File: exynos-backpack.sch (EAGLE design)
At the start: 53 parts, among them IC1 MIC5335-SPYMT, IC2 TXS0108ERGY, IC3 LTC4352DD, IC4 LTC4352DD, IC5 LTC4352DD, Q1 SI7234DP, Q2 SI7234DP, Q3 SI7234DP

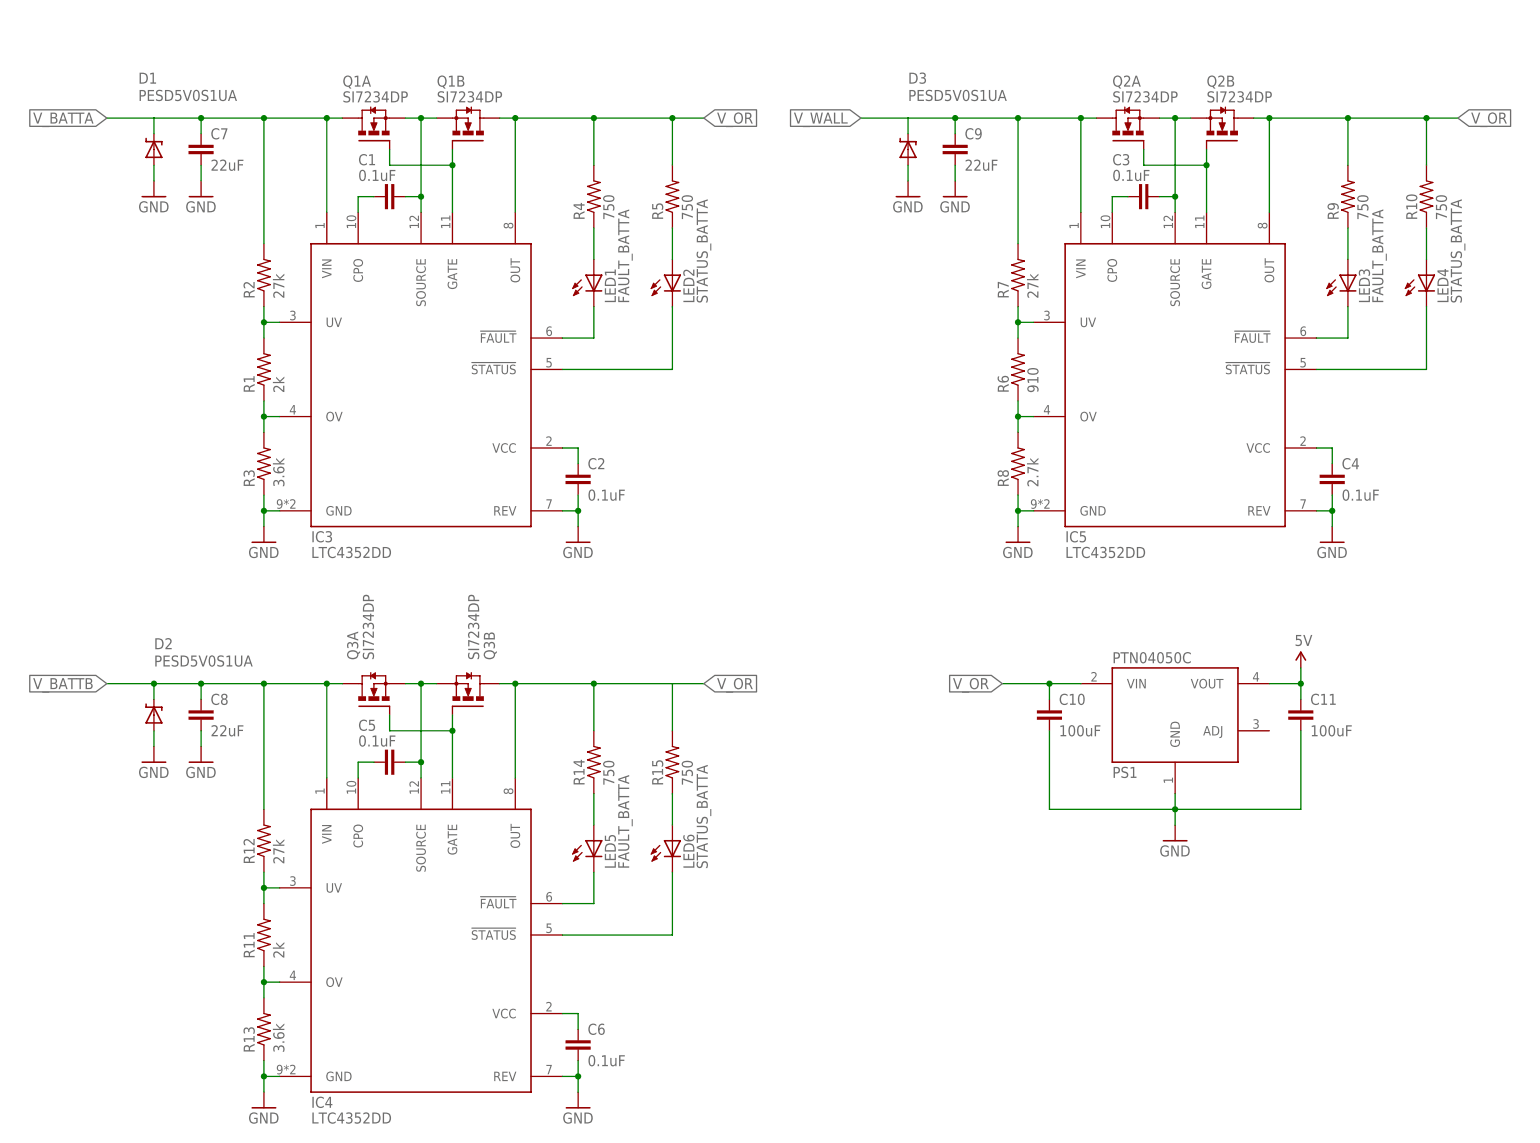
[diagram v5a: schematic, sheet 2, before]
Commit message: Adjust Rlim on LiPo ideal-OR LEDs down to 330
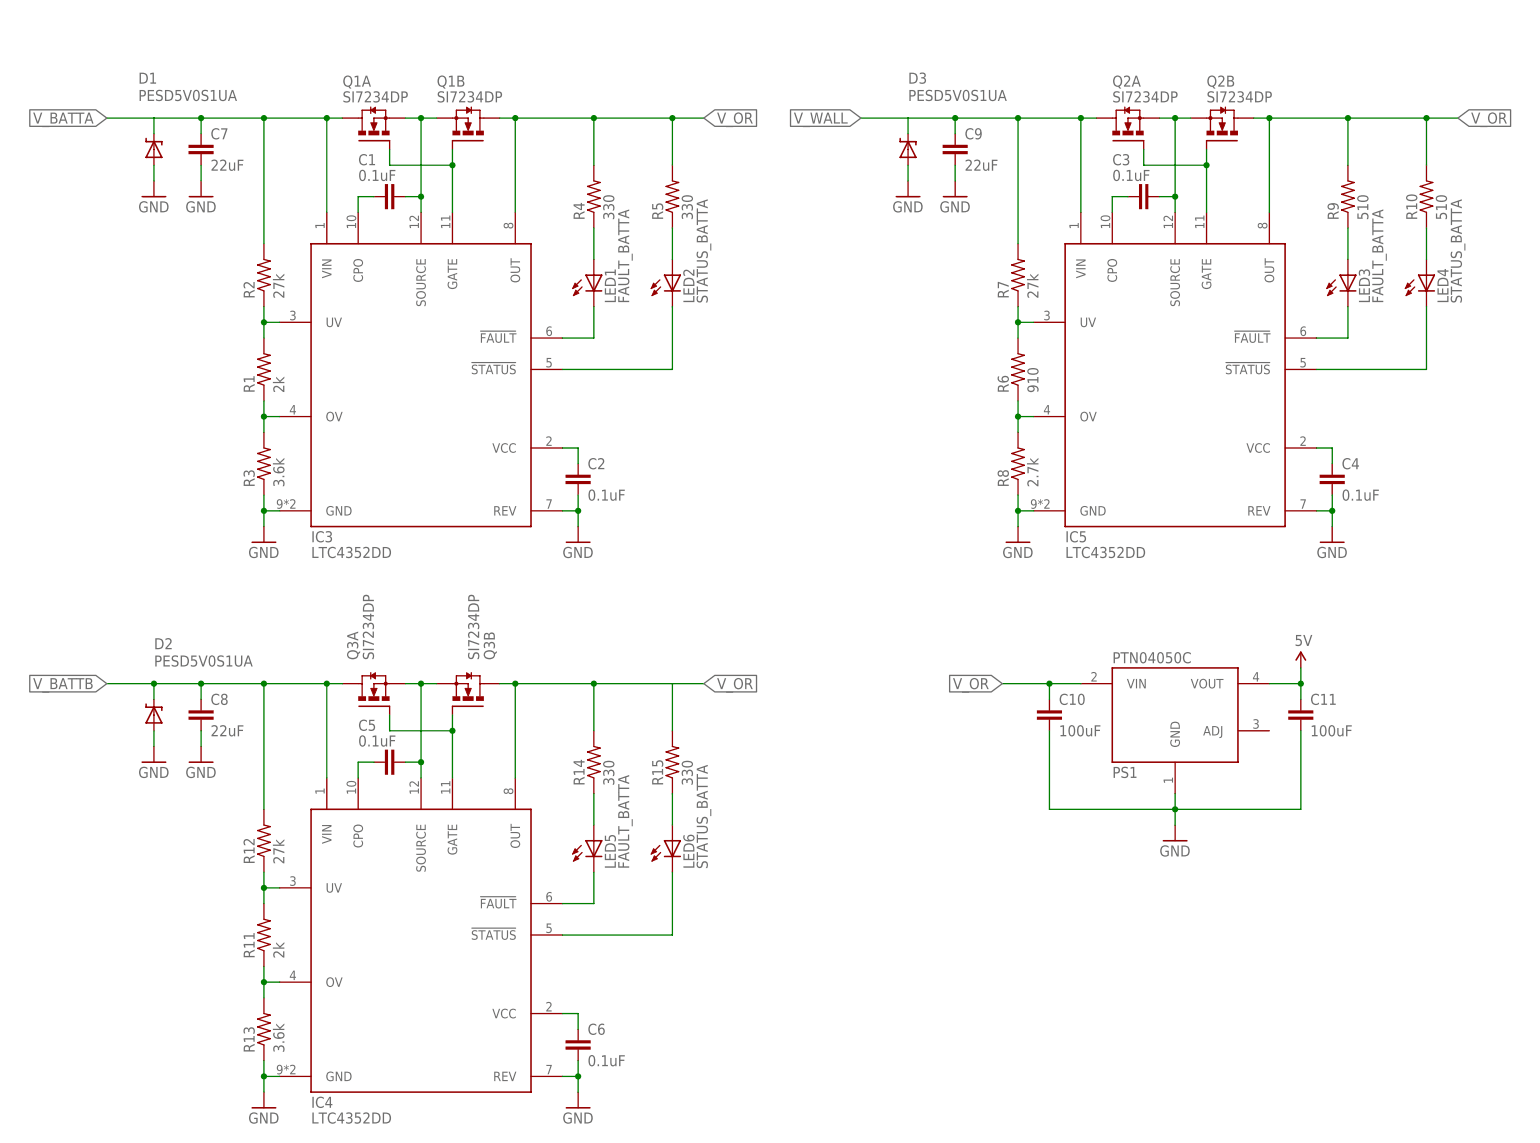
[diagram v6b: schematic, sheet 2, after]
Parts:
- R10, R9: value 750 -> 510
- R14, R15, R4, R5: value 750 -> 330
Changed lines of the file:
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@@
 <part name="C1" library="biomimetic" deviceset="CAP" device="0402-CAP" value="0.1uF"/>
 <part name="C2" library="biomimetic" deviceset="CAP" device="0402-CAP" value="0.1uF"/>
-<part name="R4" library="biomimetic" deviceset="RESISTOR" device="0402-RES" value="750"/>
-<part name="R5" library="biomimetic" deviceset="RESISTOR" device="0402-RES" value="750"/>
+<part name="R4" library="biomimetic" deviceset="RESISTOR" device="0402-RES" value="330"/>
+<part name="R5" library="biomimetic" deviceset="RESISTOR" device="0402-RES" value="330"/>
 <part name="LED1" library="biomimetic" deviceset="LED" device="0603" value="FAULT_BATTA"/>
 <part name="LED2" library="biomimetic" deviceset="LED" device="0603" value="STATUS_BATTA"/>
@@
 <part name="C3" library="biomimetic" deviceset="CAP" device="0402-CAP" value="0.1uF"/>
 <part name="C4" library="biomimetic" deviceset="CAP" device="0402-CAP" value="0.1uF"/>
-<part name="R9" library="biomimetic" deviceset="RESISTOR" device="0402-RES" value="750"/>
-<part name="R10" library="biomimetic" deviceset="RESISTOR" device="0402-RES" value="750"/>
+<part name="R9" library="biomimetic" deviceset="RESISTOR" device="0402-RES" value="510"/>
+<part name="R10" library="biomimetic" deviceset="RESISTOR" device="0402-RES" value="510"/>
 <part name="LED3" library="biomimetic" deviceset="LED" device="0603" value="FAULT_BATTA"/>
 <part name="LED4" library="biomimetic" deviceset="LED" device="0603" value="STATUS_BATTA"/>
@@
 <part name="C5" library="biomimetic" deviceset="CAP" device="0402-CAP" value="0.1uF"/>
 <part name="C6" library="biomimetic" deviceset="CAP" device="0402-CAP" value="0.1uF"/>
-<part name="R14" library="biomimetic" deviceset="RESISTOR" device="0402-RES" value="750"/>
-<part name="R15" library="biomimetic" deviceset="RESISTOR" device="0402-RES" value="750"/>
+<part name="R14" library="biomimetic" deviceset="RESISTOR" device="0402-RES" value="330"/>
+<part name="R15" library="biomimetic" deviceset="RESISTOR" device="0402-RES" value="330"/>
 <part name="LED5" library="biomimetic" deviceset="LED" device="0603" value="FAULT_BATTA"/>
 <part name="LED6" library="biomimetic" deviceset="LED" device="0603" value="STATUS_BATTA"/>

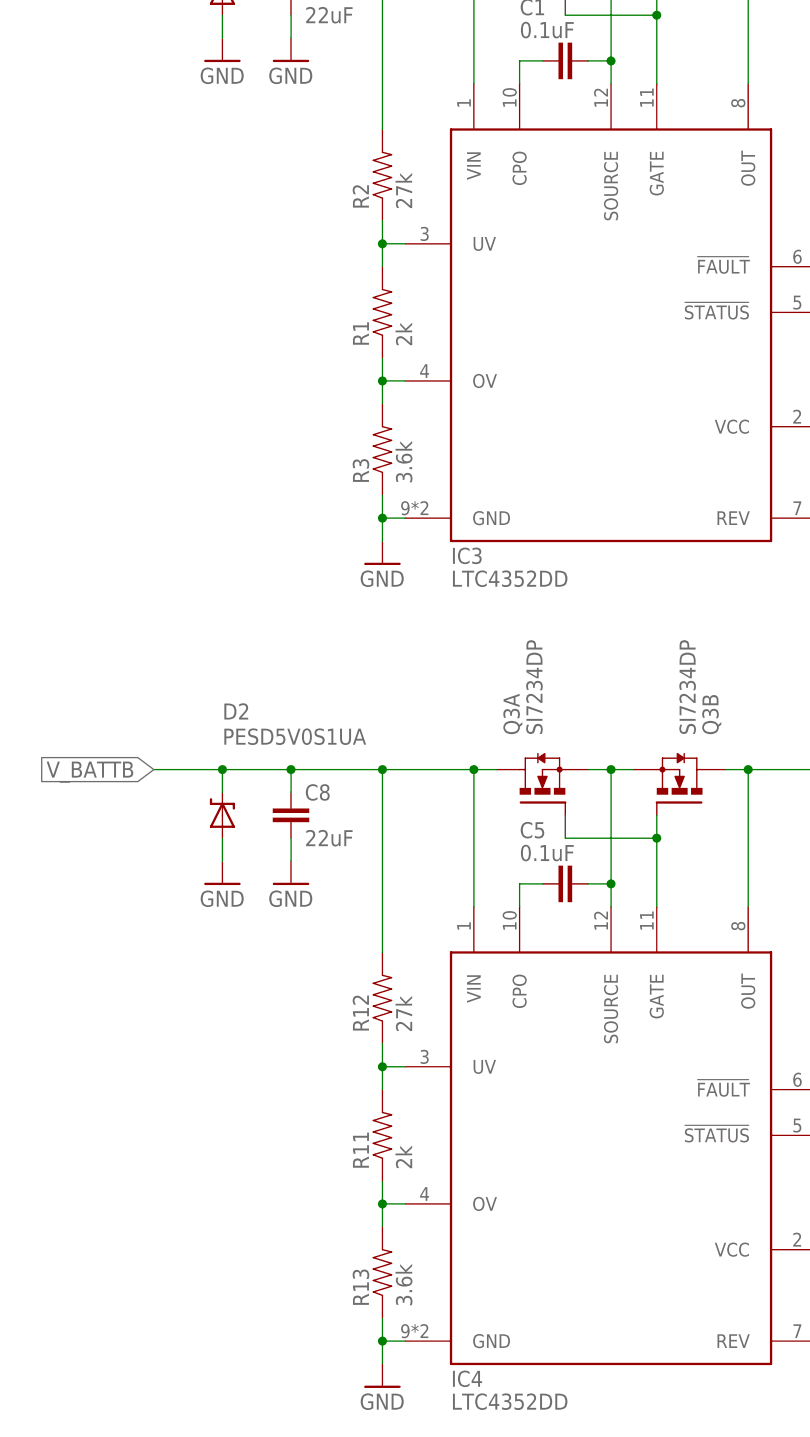
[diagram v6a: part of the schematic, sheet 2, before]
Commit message: Change OV/UV resistors to Robert Ou's values
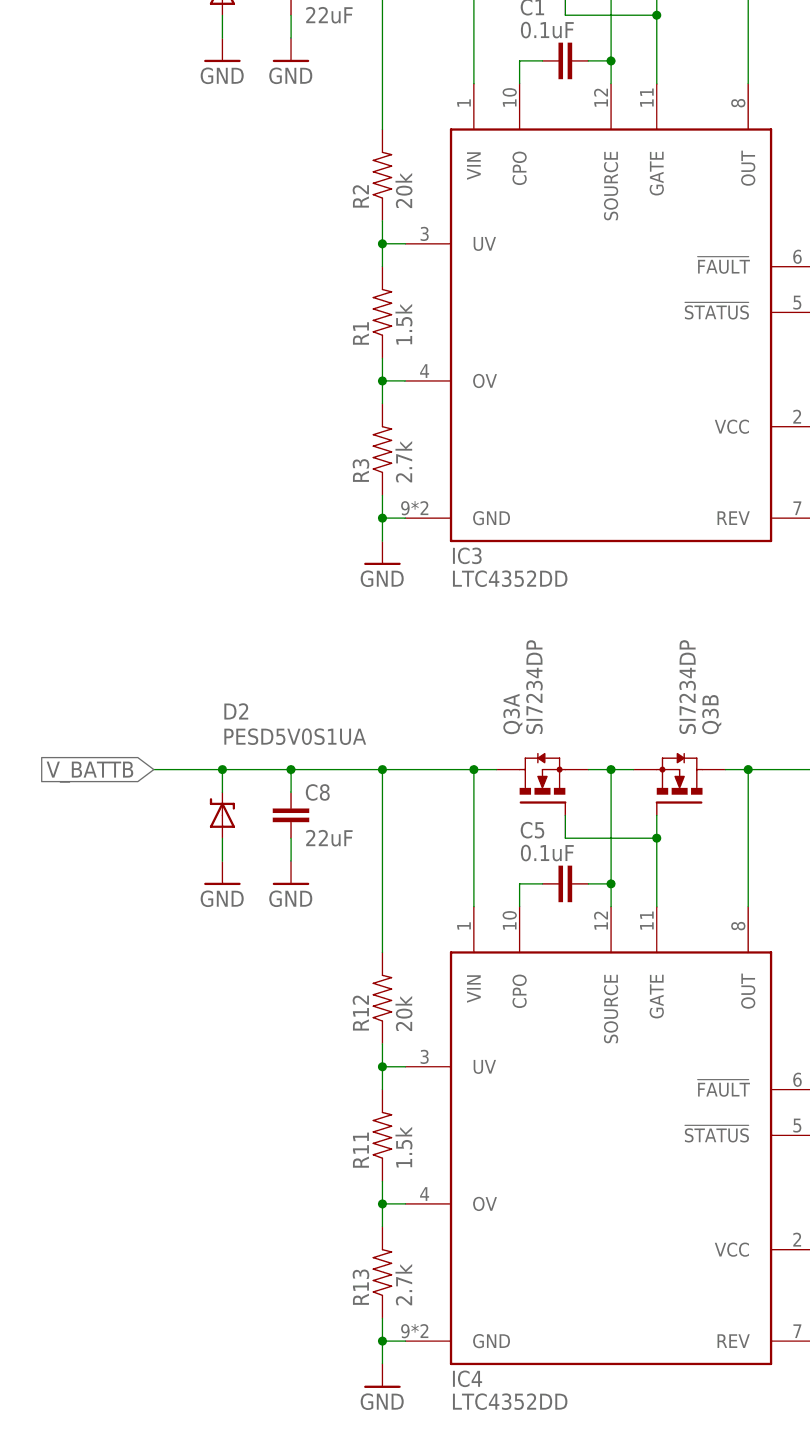
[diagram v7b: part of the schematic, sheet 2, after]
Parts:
- R1, R11: value 2k -> 1.5k
- R12, R2: value 27k -> 20k
- R13, R3: value 3.6k -> 2.7k
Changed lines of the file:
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@@
 <part name="FRAME1" library="biomimetic" deviceset="FRAME-LETTER" device=""/>
 <part name="IC3" library="biomimetic" deviceset="LTC4352" device="DD"/>
-<part name="R1" library="biomimetic" deviceset="RESISTOR" device="0402-RES" value="2k"/>
-<part name="R2" library="biomimetic" deviceset="RESISTOR" device="0402-RES" value="27k"/>
-<part name="R3" library="biomimetic" deviceset="RESISTOR" device="0402-RES" value="3.6k"/>
+<part name="R1" library="biomimetic" deviceset="RESISTOR" device="0402-RES" value="1.5k"/>
+<part name="R2" library="biomimetic" deviceset="RESISTOR" device="0402-RES" value="20k"/>
+<part name="R3" library="biomimetic" deviceset="RESISTOR" device="0402-RES" value="2.7k"/>
 <part name="Q1" library="biomimetic" deviceset="SI7234DP" device=""/>
 <part name="C1" library="biomimetic" deviceset="CAP" device="0402-CAP" value="0.1uF"/>
@@
 <part name="GND7" library="biomimetic" deviceset="GND" device=""/>
 <part name="IC4" library="biomimetic" deviceset="LTC4352" device="DD"/>
-<part name="R11" library="biomimetic" deviceset="RESISTOR" device="0402-RES" value="2k"/>
-<part name="R12" library="biomimetic" deviceset="RESISTOR" device="0402-RES" value="27k"/>
-<part name="R13" library="biomimetic" deviceset="RESISTOR" device="0402-RES" value="3.6k"/>
+<part name="R11" library="biomimetic" deviceset="RESISTOR" device="0402-RES" value="1.5k"/>
+<part name="R12" library="biomimetic" deviceset="RESISTOR" device="0402-RES" value="20k"/>
+<part name="R13" library="biomimetic" deviceset="RESISTOR" device="0402-RES" value="2.7k"/>
 <part name="Q3" library="biomimetic" deviceset="SI7234DP" device=""/>
 <part name="C5" library="biomimetic" deviceset="CAP" device="0402-CAP" value="0.1uF"/>
